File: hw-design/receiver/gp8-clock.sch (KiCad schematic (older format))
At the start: 48 parts, among them Q1 Q_NPN_BCE, Q2 Q_NPN_BCE, SW1 SW_PUSH, U1 TSOP39538, U2 weight-scale-lcd, U3 STM32F0-LQFP48, U4 usb-micro, Y1 Crystal

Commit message: Revision 2
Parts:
- added P2: test-double, iwasz:testpad-2p, symbol test-double
- added P3: CONN_01X04, w_pin_strip:pin_strip_4, symbol CONN_01X04
- added Q3: BC847, w_smd_trans:sot23, symbol Q_NPN_BCE
- added R25: Photores, photo-elements:T0-46-A10XX, symbol Photores
- added R26: 10k, w_smd_resistors:r_0603, symbol R
- added R27: 1k, w_smd_resistors:r_0603, symbol R
- added R31, R32: 22R, w_smd_resistors:r_0603, symbol R
- added SP1: BUZZER, Buzzers_Beepers:Buzzer_12x9.5RM7.6, symbol SPEAKER
- D2: footprint w_indicators:led_3mm_red -> w_indicators:led_5mm_red
- Q1, Q2: value Q_NPN_BCE -> BC847
- SW1: footprint w_switch:PCB_PUSH -> iwasz:tact-switch-smd
- U3: value STM32F0-LQFP48 -> STM32F072CB / STM32F042C6
- Y1: value Crystal -> 8MHz; footprint w_crystal:hc-49_smd -> w_crystal:crystal_hc-49s
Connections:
- net labels added: complete, progress, sound, swdclk, swdio
- wire segments 141 -> 161
- no-connect marks 3 -> 2

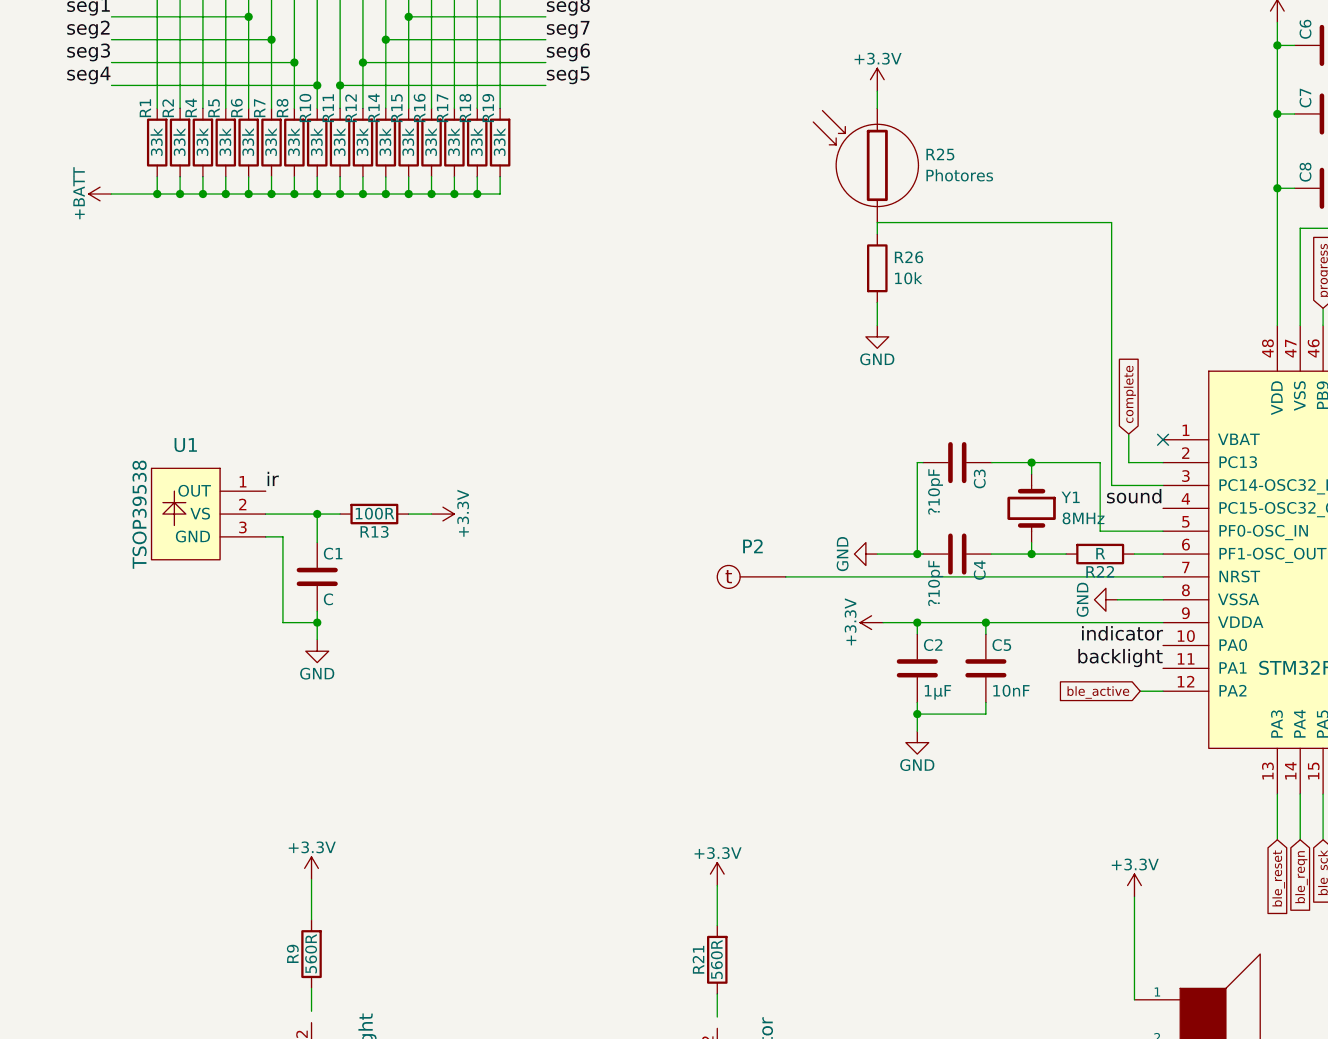
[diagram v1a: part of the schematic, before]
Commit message: Funkcjonaloność tego zegara na LEDac jest w tym momencie powtórzona na LCDku
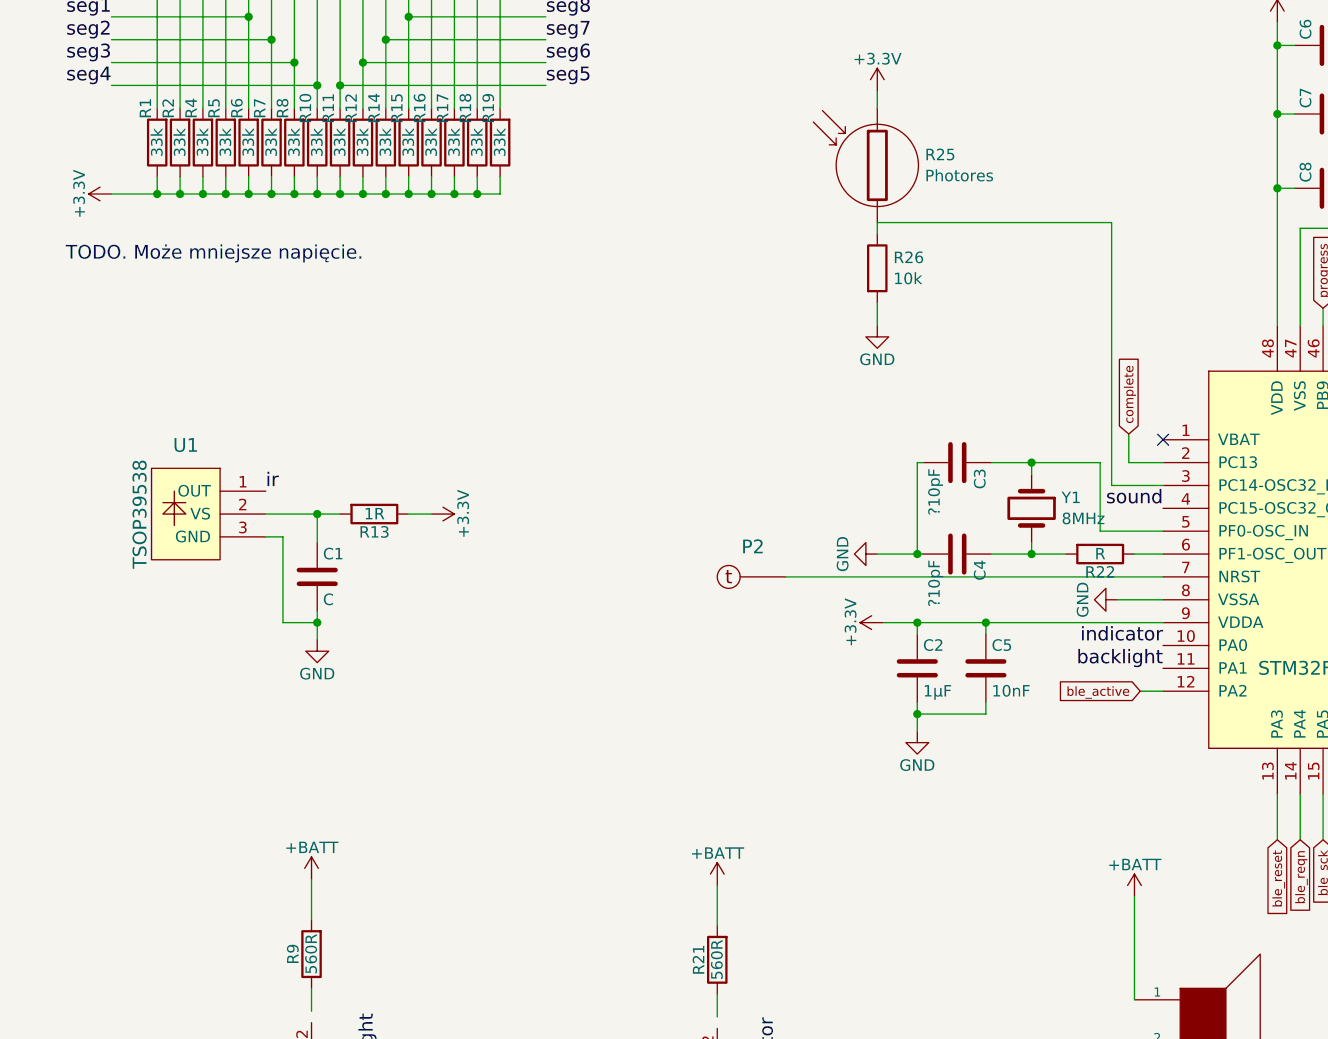
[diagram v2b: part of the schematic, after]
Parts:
- R13: value 100R -> 1R
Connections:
- net +3V3: now also R1.1, R10.1, R11.1, R12.1, R14.1, R15.1, R16.1, R17.1, R18.1, R19.1, R2.1, R4.1, R5.1, R6.1, R7.1, R8.1; no longer R21.2, R9.2, SP1.1
- net +BATT: now also R21.2, R9.2, SP1.1; no longer R1.1, R10.1, R11.1, R12.1, R14.1, R15.1, R16.1, R17.1, R18.1, R19.1, R2.1, R4.1, R5.1, R6.1, R7.1, R8.1
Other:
- note added: "TODO. Może mniejsze napięcie."
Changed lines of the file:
@@
 	0    -1   -1   0
-$EndComp
-$Comp
-L +3.3V #PWR012
-U 1 1 5633D97C
-P 1775 5800
-F 0 "#PWR012" H 1775 5650 50  0001 C CNN
-F 1 "+3.3V" H 1775 5940 50  0000 C CNN
-F 2 "" H 1775 5800 60  0000 C CNN
-F 3 "" H 1775 5800 60  0000 C CNN
-	1    1775 5800
-	1    0    0    -1
 $EndComp
 Text Label 1025 7050 2    60   ~ 0
@@
 	1    1100 2575
 	-1   0    0    1
-$EndComp
-$Comp
-L +BATT #PWR013
-U 1 1 5633F577
-P 900 2800
-F 0 "#PWR013" H 900 2650 50  0001 C CNN
-F 1 "+BATT" H 900 2940 50  0000 C CNN
-F 2 "" H 900 2800 60  0000 C CNN
-F 3 "" H 900 2800 60  0000 C CNN
-	1    900  2800
-	0    -1   -1   0
 $EndComp
 $Comp
@@
 P 2050 4200
 F 0 "R13" V 2130 4200 50  0000 C CNN
-F 1 "100R" V 2050 4200 50  0000 C CNN
+F 1 "1R" V 2050 4200 50  0000 C CNN
 F 2 "w_smd_resistors:r_0603" V 1980 4200 30  0001 C CNN
 F 3 "" H 2050 4200 30  0000 C CNN
@@
 F 3 "" H 3450 7100 60  0000 C CNN
 	1    3450 7100
-	1    0    0    -1
-$EndComp
-$Comp
-L +3.3V #PWR018
-U 1 1 56398CB1
-P 3550 5825
-F 0 "#PWR018" H 3550 5675 50  0001 C CNN
-F 1 "+3.3V" H 3550 5965 50  0000 C CNN
-F 2 "" H 3550 5825 60  0000 C CNN
-F 3 "" H 3550 5825 60  0000 C CNN
-	1    3550 5825
 	1    0    0    -1
 $EndComp
@@
 $EndComp
 $Comp
-L +3.3V #PWR026
-U 1 1 56896E16
-P 5375 5875
-F 0 "#PWR026" H 5375 5725 50  0001 C CNN
-F 1 "+3.3V" H 5375 6015 50  0000 C CNN
-F 2 "" H 5375 5875 60  0000 C CNN
-F 3 "" H 5375 5875 60  0000 C CNN
-	1    5375 5875
-	1    0    0    -1
-$EndComp
-$Comp
 L R R27
 U 1 1 56896E1C
@@
 	1    0    0    -1
 $EndComp
+$Comp
+L +BATT #PWR?
+U 1 1 56A9F06D
+P 1775 5800
+F 0 "#PWR?" H 1775 5650 50  0001 C CNN
+F 1 "+BATT" H 1775 5940 50  0000 C CNN
+F 2 "" H 1775 5800 60  0000 C CNN
+F 3 "" H 1775 5800 60  0000 C CNN
+	1    1775 5800
+	1    0    0    -1
+$EndComp
+$Comp
+L +BATT #PWR?
+U 1 1 56AA0BAF
+P 3550 5825
+F 0 "#PWR?" H 3550 5675 50  0001 C CNN
+F 1 "+BATT" H 3550 5965 50  0000 C CNN
+F 2 "" H 3550 5825 60  0000 C CNN
+F 3 "" H 3550 5825 60  0000 C CNN
+	1    3550 5825
+	1    0    0    -1
+$EndComp
+$Comp
+L +BATT #PWR?
+U 1 1 56AA0ED8
+P 5375 5875
+F 0 "#PWR?" H 5375 5725 50  0001 C CNN
+F 1 "+BATT" H 5375 6015 50  0000 C CNN
+F 2 "" H 5375 5875 60  0000 C CNN
+F 3 "" H 5375 5875 60  0000 C CNN
+	1    5375 5875
+	1    0    0    -1
+$EndComp
+Text Notes 700  3100 0    60   ~ 0
+TODO. Może mniejsze napięcie.
+$Comp
+L +3.3V #PWR?
+U 1 1 56AA410F
+P 900 2800
+F 0 "#PWR?" H 900 2650 50  0001 C CNN
+F 1 "+3.3V" H 900 2940 50  0000 C CNN
+F 2 "" H 900 2800 60  0000 C CNN
+F 3 "" H 900 2800 60  0000 C CNN
+	1    900  2800
+	0    -1   -1   0
+$EndComp
 $EndSCHEMATC

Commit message: HW changes, removed BLE, and changed chanrging and ldo circuits
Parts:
- removed R1, R10, R11, R12, R14, R15, R16, R17, R18, R19, R2, R4, R5, R6, R7, R8: 33k, w_smd_resistors:r_0603, symbol R
- added U?: PCF85176T, symbol PCF85176T
- R22: value R -> 220R
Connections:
- net GND: now also U?.49 (OSC), U?.50 (A0), U?.51 (A1), U?.52 (A2), U?.53 (SA0), U?.54 (VSS)
- net com1: no longer U2.1 (COM1)
- net com2: no longer U2.2 (COM2)
- net com3: no longer U2.3 (COM3)
- net com4: no longer U2.4 (COM4)
- net seg1: no longer U2.5
- net seg10: no longer U2.14
- net seg11: no longer U2.15
- net seg12: no longer U2.16
- net seg2: no longer U2.6
- net seg3: no longer U2.7
- net seg4: no longer U2.8
- net seg5: no longer U2.9
- net seg6: no longer U2.10
- net seg7: no longer U2.11
- net seg8: no longer U2.12
- net seg9: no longer U2.13
- net at D1.1 (K): now also Q1.2 (C)
- net at D1.2 (A): now also R9.1
- net at D2.1 (K): now also Q2.2 (C)
- net at D2.2 (A): now also R21.1
- net ble_miso: no longer names the net of U3.16 (PA6)
- net ble_mosi: no longer names the net of U3.17 (PA7)
- net ble_rdyn: no longer names the net of U3.18 (PB0)
- net ble_reqn: no longer names the net of U3.14 (PA4)
- net ble_reset: no longer names the net of U3.13 (PA3)
- net ble_sck: no longer names the net of U3.15 (PA5)
- new net: U2.1 (COM1), U?.56 (BP0)
- new net: U2.10, U?.9 (S5)
- new net: U2.11, U?.10 (S6)
- new net: U2.12, U?.11 (S7)
- new net: U2.13, U?.12 (S8)
- new net: U2.14, U?.13 (S9)
- new net: U2.15, U?.14 (S10)
- new net: U2.16, U?.15 (S11)
- new net: U2.2 (COM2), U?.2 (BP1)
- new net: U2.3 (COM3), U?.1 (BP2)
- new net: U2.4 (COM4), U?.3 (BP3)
- new net: U2.5, U?.4 (S0)
- new net: U2.6, U?.5 (S1)
- new net: U2.7, U?.6 (S2)
- new net: U2.8, U?.7 (S3)
- new net: U2.9, U?.8 (S4)
- no-connect marks 2 -> 38
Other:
- note removed: "TODO. Może mniejsze napięcie."
- moved on the sheet: U2

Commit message: 2017 improvements
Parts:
- removed D2: LED, w_indicators:led_5mm_red, symbol LED
- removed Q2: BC847, w_smd_trans:sot23, symbol Q_NPN_BCE
- removed R20: 1k, w_smd_resistors:r_0603, symbol R
- removed R21: 560R, w_smd_resistors:r_0603, symbol R
- removed U2: weight-scale-lcd, iwasz:weight-scale-lcd, symbol weight-scale-lcd
- removed U?: PCF85176T, symbol PCF85176T
- added J1, J10, J11, J12: CONN_01X01, Mounting_Holes:MountingHole_3.2mm_M3_DIN965_Pad, symbol CONN_01X01
- added J2, J3, J4, J5, J6, J7, J8, J9: CONN_01X01, Pin_Headers:Pin_Header_Straight_1x01_Pitch2.00mm, symbol CONN_01X01
- added P6: CONN_01X04, w_pin_strip:pin_strip_2mm_4, symbol CONN_01X04
- added R1: 10k, w_smd_resistors:r_0603, symbol R
- P3: footprint w_pin_strip:pin_strip_4 -> w_pin_strip:pin_strip_2mm_4
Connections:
- net GND: now also P6.3 (P3), R1.2
- net sense: now reaches U3.13 (PA3)
- net at U3.44 (BOOT0-PF11): now also R1.1
- net nrst: now reaches P2.1 (T), U3.7 (NRST)
- net nrst: now also P6.4 (P4)
- net ble_active: no longer names the net of U3.12 (PA2)
- net com1: no longer names the net of U3.20 (PB2)
- net com2: no longer names the net of U3.21 (PB10)
- net com3: no longer names the net of U3.22 (PB11)
- net com4: no longer names the net of U3.25 (PB12)
- net complete renamed Sheet56372EC5/complete
- net indicator: no longer names the net of U3.10 (PA0)
- net progress renamed Sheet56372EC5/progress
- net seg1: no longer names the net of U3.26 (PB13)
- net seg10: no longer names the net of U3.41 (PB5)
- net seg11 renamed screen/scl
- net seg12 renamed screen/sda
- net seg2: no longer names the net of U3.27 (PB14)
- net seg3: no longer names the net of U3.28 (PB15)
- net seg4: no longer names the net of U3.29 (PA8)
- net seg5 renamed consoleTx
- net consoleTx: now also P6.1 (P1)
- net seg6 renamed consoleRx
- net consoleRx: now also P6.2 (P2)
- net seg7: no longer names the net of U3.38 (PA15)
- net seg8: no longer names the net of U3.39 (PB3)
- net seg9: no longer names the net of U3.40 (PB4)
- no-connect marks 38 -> 21
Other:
- note removed: "Indicator"
- note removed: "LCD screen"
- moved on the sheet: P3, R31, R32
